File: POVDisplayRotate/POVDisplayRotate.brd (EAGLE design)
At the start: 52 x 86 mm, 49 parts, among them U1 STP08DP05, U2 STP08DP05, U3 MPQ4420Q, U4 CY8CKIT-142, U5 M95M01

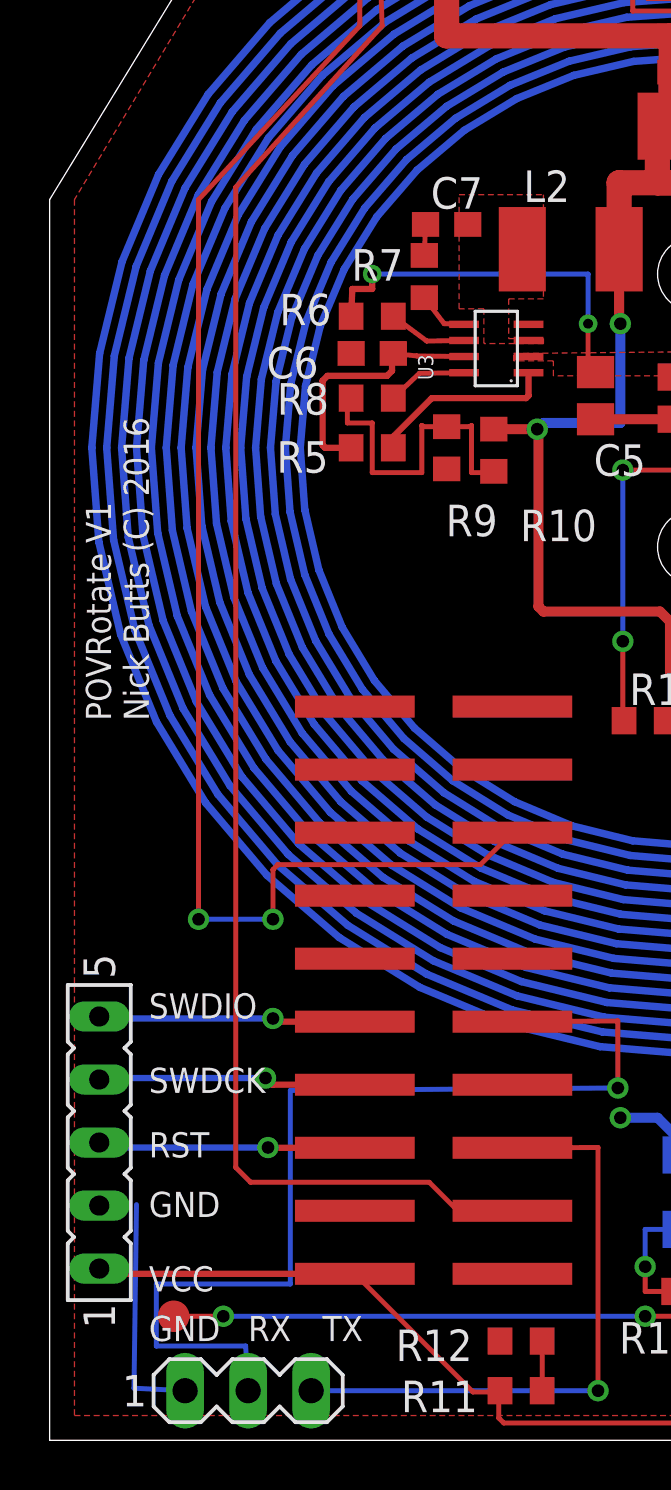
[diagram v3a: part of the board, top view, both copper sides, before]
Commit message: Order Oshpark boards for POV Rotate and POV Base
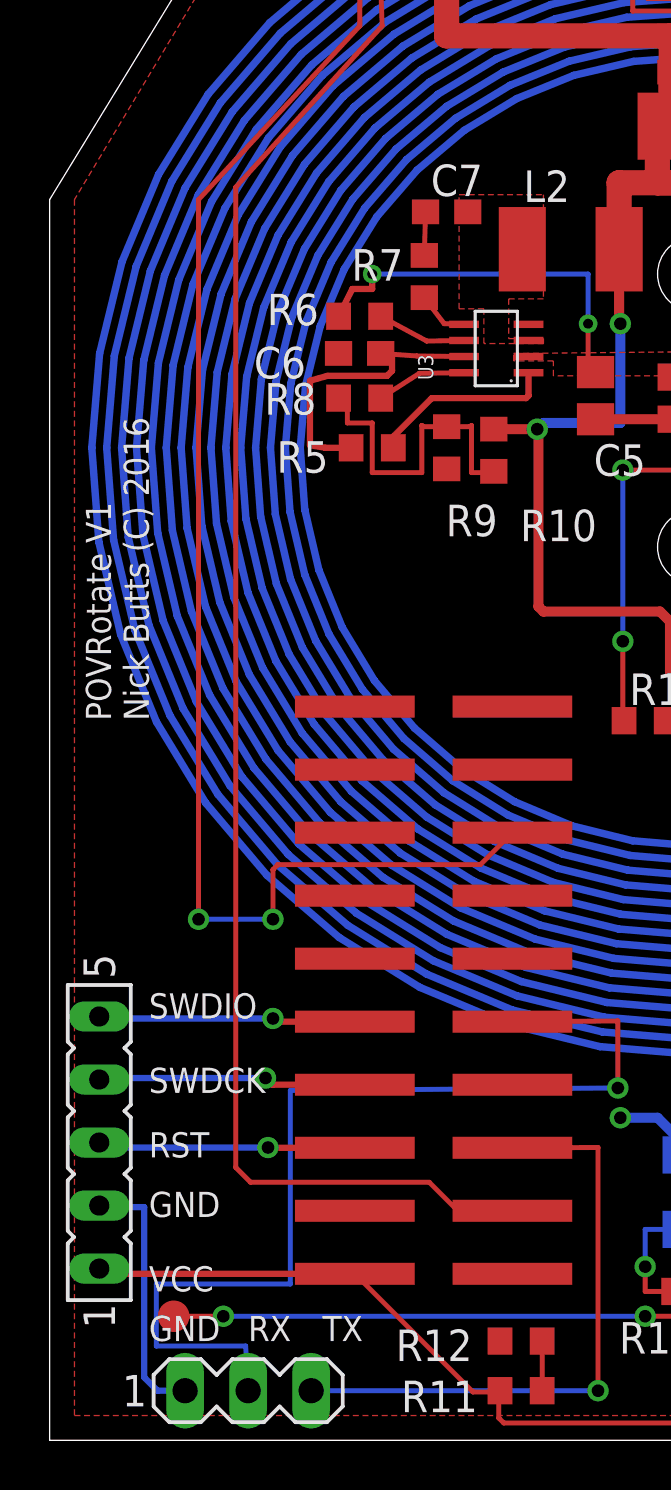
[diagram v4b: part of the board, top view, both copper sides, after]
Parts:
- moved C7 0.51 mm to (16.0, 49.5)
- moved C6 0.51 mm to (12.5, 43.8)
- moved R6 0.51 mm to (12.5, 45.3)
- moved R8 0.51 mm to (12.5, 42.0)
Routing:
- net N$1: track 10.3 -> 12.2 mm
- net GND: track 22.6 -> 23.7 mm
- net N$8: track 1.25 -> 1.76 mm
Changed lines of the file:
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@@
 <grid distance="0.05" unitdist="inch" unit="inch" style="lines" multiple="1" display="yes" altdistance="0.005" altunitdist="inch" altunit="inch"/>
 <layers>
-<layer number="1" name="Top" color="4" fill="1" visible="no" active="yes"/>
-<layer number="16" name="Bottom" color="1" fill="1" visible="no" active="yes"/>
+<layer number="1" name="Top" color="4" fill="1" visible="yes" active="yes"/>
+<layer number="16" name="Bottom" color="1" fill="1" visible="yes" active="yes"/>
 <layer number="17" name="Pads" color="2" fill="1" visible="yes" active="yes"/>
-<layer number="18" name="Vias" color="2" fill="1" visible="no" active="yes"/>
-<layer number="19" name="Unrouted" color="6" fill="1" visible="no" active="yes"/>
+<layer number="18" name="Vias" color="2" fill="1" visible="yes" active="yes"/>
+<layer number="19" name="Unrouted" color="6" fill="1" visible="yes" active="yes"/>
 <layer number="20" name="Dimension" color="15" fill="1" visible="yes" active="yes"/>
 <layer number="21" name="tPlace" color="16" fill="1" visible="yes" active="yes"/>
-<layer number="22" name="bPlace" color="14" fill="1" visible="no" active="yes"/>
-<layer number="23" name="tOrigins" color="15" fill="1" visible="no" active="yes"/>
-<layer number="24" name="bOrigins" color="15" fill="1" visible="no" active="yes"/>
+<layer number="22" name="bPlace" color="14" fill="1" visible="yes" active="yes"/>
+<layer number="23" name="tOrigins" color="15" fill="1" visible="yes" active="yes"/>
+<layer number="24" name="bOrigins" color="15" fill="1" visible="yes" active="yes"/>
 <layer number="25" name="tNames" color="7" fill="1" visible="no" active="yes"/>
 <layer number="26" name="bNames" color="7" fill="1" visible="no" active="yes"/>
-<layer number="27" name="tValues" color="7" fill="1" visible="yes" active="yes"/>
+<layer number="27" name="tValues" color="7" fill="1" visible="no" active="yes"/>
 <layer number="28" name="bValues" color="7" fill="1" visible="no" active="yes"/>
 <layer number="29" name="tStop" color="7" fill="3" visible="no" active="yes"/>
 <layer number="30" name="bStop" color="7" fill="6" visible="no" active="yes"/>
-<layer number="31" name="tCream" color="7" fill="4" visible="yes" active="yes"/>
+<layer number="31" name="tCream" color="7" fill="4" visible="no" active="yes"/>
 <layer number="32" name="bCream" color="7" fill="5" visible="no" active="yes"/>
 <layer number="33" name="tFinish" color="6" fill="3" visible="no" active="yes"/>
@@
 <attribute name="DIGIKEY" value="160-2162-1-ND" x="26" y="60" size="1.778" layer="27" rot="R90" display="off"/>
 </element>
-<element name="R8" library="resistor" package="R0603" value="51k" x="13" y="42" smashed="yes">
-<attribute name="DIGIKEY" value="P0.0GCT-ND" x="13" y="42" size="1.778" layer="27" display="off"/>
-<attribute name="NAME" x="9.165" y="41.335" size="1.27" layer="25"/>
-<attribute name="VALUE" x="12.365" y="40.095" size="1.27" layer="27"/>
+<element name="R8" library="resistor" package="R0603" value="51k" x="12.492" y="42" smashed="yes">
+<attribute name="DIGIKEY" value="P0.0GCT-ND" x="12.492" y="42" size="1.778" layer="27" display="off"/>
+<attribute name="NAME" x="8.657" y="41.335" size="1.27" layer="25"/>
+<attribute name="VALUE" x="11.857" y="40.095" size="1.27" layer="27"/>
 </element>
 <element name="C9" library="resistor" package="C1210" value="100u" x="25.89" y="52.96" smashed="yes">
@@
 <attribute name="VALUE" x="20.54" y="42.73" size="0.6096" layer="27" rot="R90"/>
 </element>
-<element name="C6" library="resistor" package="C0603" value="0.1u" x="13" y="43.8" smashed="yes" rot="R180">
-<attribute name="DIGIKEY" value="490-6505-1-ND" x="13" y="43.8" size="1.778" layer="27" rot="R180" display="off"/>
-<attribute name="NAME" x="10.835" y="44.065" size="1.27" layer="25" rot="R180"/>
-<attribute name="VALUE" x="13.635" y="45.705" size="1.27" layer="27" rot="R180"/>
-</element>
-<element name="R6" library="resistor" package="R0603" value="1M" x="13" y="45.3" smashed="yes">
-<attribute name="DIGIKEY" value="P0.0GCT-ND" x="13" y="45.3" size="1.778" layer="27" font="vector" ratio="15" display="off"/>
-<attribute name="NAME" x="9.265" y="44.935" size="1.27" layer="25"/>
-<attribute name="VALUE" x="12.365" y="43.395" size="1.27" layer="27"/>
+<element name="C6" library="resistor" package="C0603" value="0.1u" x="12.492" y="43.8" smashed="yes" rot="R180">
+<attribute name="DIGIKEY" value="490-6505-1-ND" x="12.492" y="43.8" size="1.778" layer="27" rot="R180" display="off"/>
+<attribute name="NAME" x="10.327" y="44.065" size="1.27" layer="25" rot="R180"/>
+<attribute name="VALUE" x="13.127" y="45.705" size="1.27" layer="27" rot="R180"/>
+</element>
+<element name="R6" library="resistor" package="R0603" value="1M" x="12.492" y="45.3" smashed="yes">
+<attribute name="DIGIKEY" value="P0.0GCT-ND" x="12.492" y="45.3" size="1.778" layer="27" font="vector" ratio="15" display="off"/>
+<attribute name="NAME" x="8.757" y="44.935" size="1.27" layer="25"/>
+<attribute name="VALUE" x="11.857" y="43.395" size="1.27" layer="27"/>
 </element>
 <element name="R10" library="resistor" package="R0603" value="41.2k" x="17.9" y="39.9" smashed="yes" rot="R270">
@@
 <attribute name="VALUE" x="13.195" y="47.535" size="1.27" layer="27" rot="R270"/>
 </element>
-<element name="C7" library="resistor" package="C0603" value="100n" x="16" y="49" smashed="yes">
-<attribute name="NAME" x="15.365" y="49.635" size="1.27" layer="25"/>
-<attribute name="VALUE" x="15.365" y="47.095" size="1.27" layer="27"/>
+<element name="C7" library="resistor" package="C0603" value="100n" x="16" y="49.508" smashed="yes">
+<attribute name="NAME" x="15.365" y="50.143" size="1.27" layer="25"/>
+<attribute name="VALUE" x="15.365" y="47.603" size="1.27" layer="27"/>
 </element>
 <element name="L2" library="resistor" package="L1812" value="10u" x="21" y="48" smashed="yes">
@@
 <contactref element="C6" pad="1"/>
 <wire x1="16.7" y1="43.675" x2="14.8" y2="43.7" width="0.2" layer="1"/>
-<wire x1="14.8" y1="43.7" x2="13.85" y2="43.8" width="0.2" layer="1"/>
+<wire x1="14.8" y1="43.7" x2="13.342" y2="43.8" width="0.2" layer="1"/>
 <contactref element="R5" pad="2"/>
 <wire x1="12.15" y1="40" x2="11.1" y2="40" width="0.254" layer="1"/>
-<wire x1="11.1" y1="40" x2="11" y2="40.1" width="0.254" layer="1"/>
-<wire x1="11" y1="40.1" x2="11" y2="42.7" width="0.254" layer="1"/>
-<wire x1="11" y1="42.7" x2="11.2" y2="42.9" width="0.254" layer="1"/>
+<wire x1="11.1" y1="40" x2="10.492" y2="40.1" width="0.254" layer="1"/>
+<wire x1="10.492" y1="40.1" x2="10.492" y2="42.7" width="0.254" layer="1"/>
+<wire x1="10.492" y1="42.7" x2="11.2" y2="42.9" width="0.254" layer="1"/>
 <wire x1="11.2" y1="42.9" x2="13.6" y2="42.9" width="0.254" layer="1"/>
 <wire x1="13.6" y1="42.9" x2="13.8" y2="43.1" width="0.254" layer="1"/>
 <wire x1="13.8" y1="43.1" x2="13.8" y2="43.75" width="0.254" layer="1"/>
-<wire x1="13.8" y1="43.75" x2="13.85" y2="43.8" width="0.254" layer="1"/>
+<wire x1="13.8" y1="43.75" x2="13.342" y2="43.8" width="0.254" layer="1"/>
 </signal>
 <signal name="N$2">
@@
 <contactref element="R6" pad="2"/>
 <wire x1="16.7" y1="44.325" x2="15.2" y2="44.3" width="0.2" layer="1"/>
-<wire x1="15.2" y1="44.3" x2="13.85" y2="45.3" width="0.2" layer="1"/>
+<wire x1="15.2" y1="44.3" x2="13.342" y2="45.3" width="0.2" layer="1"/>
 </signal>
 <signal name="N$4">
@@
 <contactref element="R8" pad="2"/>
 <wire x1="16.7" y1="43.025" x2="14.9" y2="43" width="0.2" layer="1"/>
-<wire x1="14.9" y1="43" x2="13.85" y2="42" width="0.2" layer="1"/>
+<wire x1="14.9" y1="43" x2="13.342" y2="42" width="0.2" layer="1"/>
 </signal>
 <signal name="N$5">
@@
 <wire x1="17" y1="40.9" x2="16.95" y2="40.85" width="0.2" layer="1"/>
 <wire x1="16.95" y1="40.85" x2="16" y2="40.85" width="0.2" layer="1"/>
-<wire x1="12.15" y1="42" x2="12" y2="41.85" width="0.2" layer="1"/>
+<wire x1="11.642" y1="42" x2="12" y2="41.85" width="0.2" layer="1"/>
 <wire x1="12" y1="41.85" x2="12" y2="41" width="0.2" layer="1"/>
 <wire x1="12" y1="41" x2="13" y2="41" width="0.2" layer="1"/>
@@
 <contactref element="R7" pad="1"/>
 <contactref element="C7" pad="1"/>
-<wire x1="15.15" y1="49" x2="15.1" y2="47.75" width="0.2" layer="1"/>
+<wire x1="15.15" y1="49.508" x2="15.1" y2="47.75" width="0.2" layer="1"/>
 </signal>
 <signal name="SWOUT">
@@
 <wire x1="34" y1="62.4" x2="34" y2="65" width="0.2" layer="1"/>
 <contactref element="SV2" pad="1"/>
-<wire x1="5.46" y1="2" x2="3.4" y2="2.1" width="0.2" layer="16"/>
-<wire x1="3.4" y1="2.1" x2="3.5" y2="9.5" width="0.2" layer="16"/>
-<wire x1="2" y1="9.46" x2="3.5" y2="9.5" width="0" layer="19" extent="16-16"/>
+<wire x1="5.46" y1="2" x2="4.35" y2="2" width="0.254" layer="16"/>
+<wire x1="4.35" y1="2" x2="3.81" y2="2.54" width="0.254" layer="16"/>
+<wire x1="3.81" y1="2.54" x2="3.81" y2="9.398" width="0.254" layer="16"/>
+<wire x1="3.81" y1="9.398" x2="2.062" y2="9.398" width="0.254" layer="16"/>
+<wire x1="2.062" y1="9.398" x2="2" y2="9.46" width="0.254" layer="16"/>
 </signal>
 <signal name="EE_MISO">
@@
 <wire x1="13" y1="47" x2="13" y2="46.4" width="0.254" layer="1"/>
 <wire x1="13" y1="46.4" x2="12.2" y2="46.4" width="0.254" layer="1"/>
-<wire x1="12.2" y1="46.4" x2="12.15" y2="45.3" width="0.254" layer="1"/>
+<wire x1="12.2" y1="46.4" x2="11.642" y2="45.3" width="0.254" layer="1"/>
 <wire x1="23.15" y1="29" x2="23.1" y2="29.05" width="0.2" layer="1"/>
 <wire x1="23.1" y1="29.05" x2="23.1" y2="32.2" width="0.2" layer="1"/>

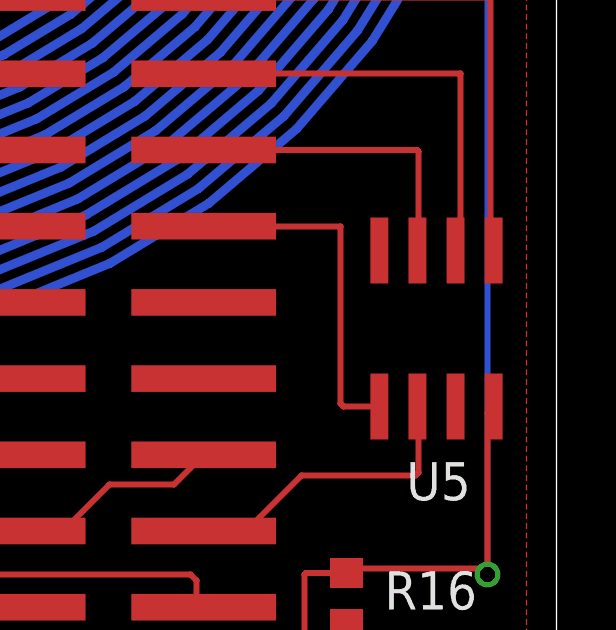
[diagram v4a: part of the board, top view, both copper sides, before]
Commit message: Updated the library and POVDisplay board with part numbers.
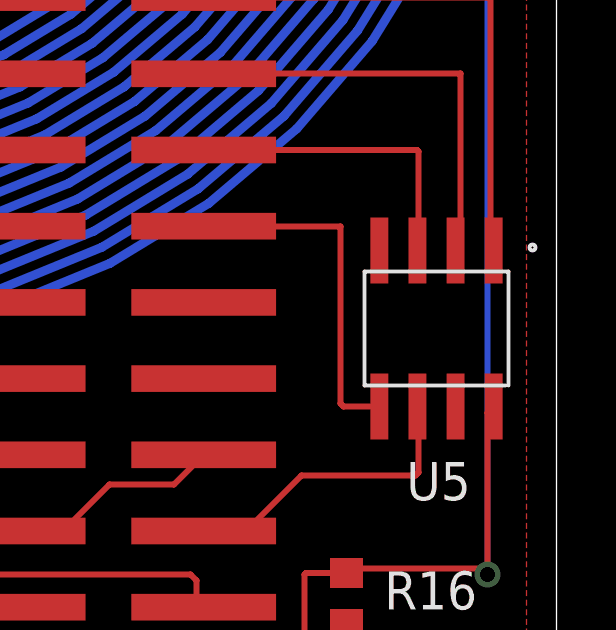
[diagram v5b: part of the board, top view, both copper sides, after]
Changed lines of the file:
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@@
 <attribute name="NAME" x="17.825" y="63.175" size="1.27" layer="25"/>
 <attribute name="VALUE" x="16.825" y="63.555" size="1.27" layer="27"/>
+<attribute name="DIGIKEY" value="497-6119-1-ND" x="20" y="68" size="1.778" layer="27" display="off"/>
 </element>
 <element name="U2" library="NicksParts" package="SSOP16_EPAD" value="STP08DP05" x="37" y="60" smashed="yes">
 <attribute name="NAME" x="34.825" y="55.175" size="1.27" layer="25"/>
 <attribute name="VALUE" x="33.825" y="55.555" size="1.27" layer="27"/>
+<attribute name="DIGIKEY" value="497-6119-1-ND" x="37" y="60" size="1.778" layer="27" display="off"/>
 </element>
 <element name="R1" library="resistor" package="R0603" value="386" x="20" y="72" smashed="yes" rot="R180">
@@
 <attribute name="NAME" x="15.46" y="42.73" size="0.6096" layer="25" rot="R90"/>
 <attribute name="VALUE" x="20.54" y="42.73" size="0.6096" layer="27" rot="R90"/>
+<attribute name="DIGIKEY" value="1589-1293-1-ND" x="18" y="44" size="1.778" layer="27" rot="R90" display="off"/>
 </element>
 <element name="C6" library="resistor" package="C0603" value="0.1u" x="12.492" y="43.8" smashed="yes" rot="R180">
@@
 </signal>
 <signal name="GND">
-<contactref element="U5" pad="4"/>
 <contactref element="SV1" pad="2"/>
 <polygon width="0.2" layer="1" thermals="no">
@@
 <wire x1="3.81" y1="9.398" x2="2.062" y2="9.398" width="0.254" layer="16"/>
 <wire x1="2.062" y1="9.398" x2="2" y2="9.46" width="0.254" layer="16"/>
+<contactref element="U5" pad="4"/>
+<wire x1="34.2" y1="62.35" x2="37" y2="60" width="0" layer="19" extent="1-1"/>
+<wire x1="26.75" y1="56.6" x2="34" y2="62.4" width="0" layer="19" extent="1-1"/>
+<wire x1="26.74" y1="55.14" x2="26.75" y2="56.6" width="0" layer="19" extent="1-1"/>
+<wire x1="27.29" y1="52.96" x2="26.74" y2="55.14" width="0" layer="19" extent="1-1"/>
+<wire x1="26.71" y1="50.68" x2="27.29" y2="52.96" width="0" layer="19" extent="1-1"/>
+<wire x1="19.3" y1="44.975" x2="26.71" y2="50.68" width="0" layer="19" extent="1-1"/>
+<wire x1="22" y1="41.15" x2="19.3" y2="44.975" width="0" layer="19" extent="1-1"/>
+<wire x1="16" y1="39.15" x2="22" y2="41.15" width="0" layer="19" extent="1-1"/>
+<wire x1="11.642" y1="43.8" x2="16" y2="39.15" width="0" layer="19" extent="1-1"/>
+<wire x1="28.85" y1="29" x2="25" y2="41.15" width="0" layer="19" extent="1-1"/>
+<wire x1="33.89" y1="29.57" x2="28.85" y2="29" width="0" layer="19" extent="1-1"/>
+<wire x1="20" y1="68" x2="26.75" y2="56.6" width="0" layer="19" extent="1-1"/>
+<wire x1="17.125" y1="70.275" x2="20" y2="68" width="0" layer="19" extent="1-1"/>
+<wire x1="19.15" y1="72" x2="17.125" y2="70.275" width="0" layer="19" extent="1-1"/>
+<wire x1="46.095" y1="18.6" x2="33.89" y2="29.57" width="0" layer="19" extent="1-1"/>
+<wire x1="45" y1="2.15" x2="46.095" y2="18.6" width="0" layer="19" extent="1-1"/>
+<wire x1="40.24" y1="1.63" x2="45" y2="2.15" width="0" layer="19" extent="1-1"/>
+<wire x1="24.5" y1="13" x2="28.85" y2="29" width="0" layer="19" extent="1-16"/>
+<wire x1="18.15" y1="4" x2="23" y2="13" width="0" layer="19" extent="1-1"/>
+<wire x1="12.3" y1="9.25" x2="18.15" y2="4" width="0" layer="19" extent="1-1"/>
+<wire x1="3.81" y1="9.398" x2="12.3" y2="9.25" width="0" layer="19" extent="1-16"/>
 </signal>
 <signal name="EE_MISO">
